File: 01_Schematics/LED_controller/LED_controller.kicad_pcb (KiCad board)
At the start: 2 copper layers, 122 x 87 mm, 221 parts, among them J1 Pin, J10 TB-02, J11 TB-02, J12 TB-03, J13 TB-02, J14 PLD-14, J15 PLD-14, J16 Pin, J17 Pin, J18 Pin, J19 Pin, J2 Pin, J20 TB-03, J21 TB-03, J22 Pin, J23 Pin, J24 Pin, J25 Pin, J26 Pin, J27 Pin, J28 PLD-14, J29 PLD-14, J3 TB-03, J30 Pin, J31 Pin, J32 Pin, J33 Pin, J34 TB-03, J35 TB-03, J36 Pin, J37 Pin, J38 Pin, J39 Pin, J4 Pin, J40 Pin, J41 Pin, J42 RJ45_LED_Shielded, J43 Pin, J44 Pin, J45 Pin, J46 Pin, J47 Pin, J48 PLS-4, J49 Pin, J5 Pin, J50 Pin, J51 Pin, J52 Pin, J53 Pin, J54 Pin, J55 Pin, J56 Pin, J57 Pin, J58 Pin, J59 Pin, J6 Pin, J60 Pin, J61 Pin, J62 Pin, J63 Pin, J64 Pin, J65 Pin, J66 Pin, J67 TB-02, J7 Pin, J7-2 Pin, J8 TB-02, J9 TB-03, K1 V23092-A1012-A301, Q1 MMBF170, U1 MC34063AD, U2 UA78L12ACPK, U3 MBI6651GSD, U4 MBI6651GSD, U5 MBI6651GSD, U6 MBI6651GSD, U7 DP83848C, U8 STM32F107RCTx, Y1 25 MHz

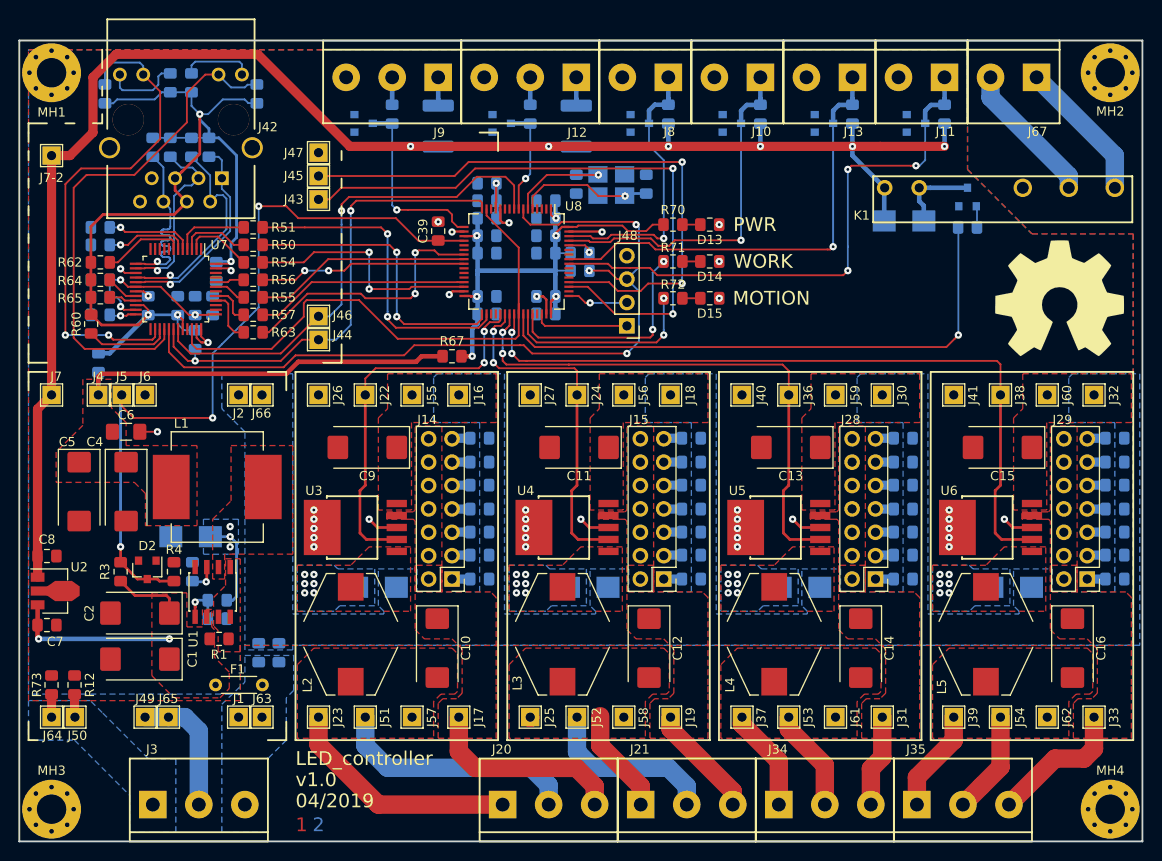
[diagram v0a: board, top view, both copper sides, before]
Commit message: - Исправлена ошибка с неправильным подключением цепи обратной связи микросхемы U1; - Плата переразведена с учетом изменений в схеме; - Добавлен файл BOM;
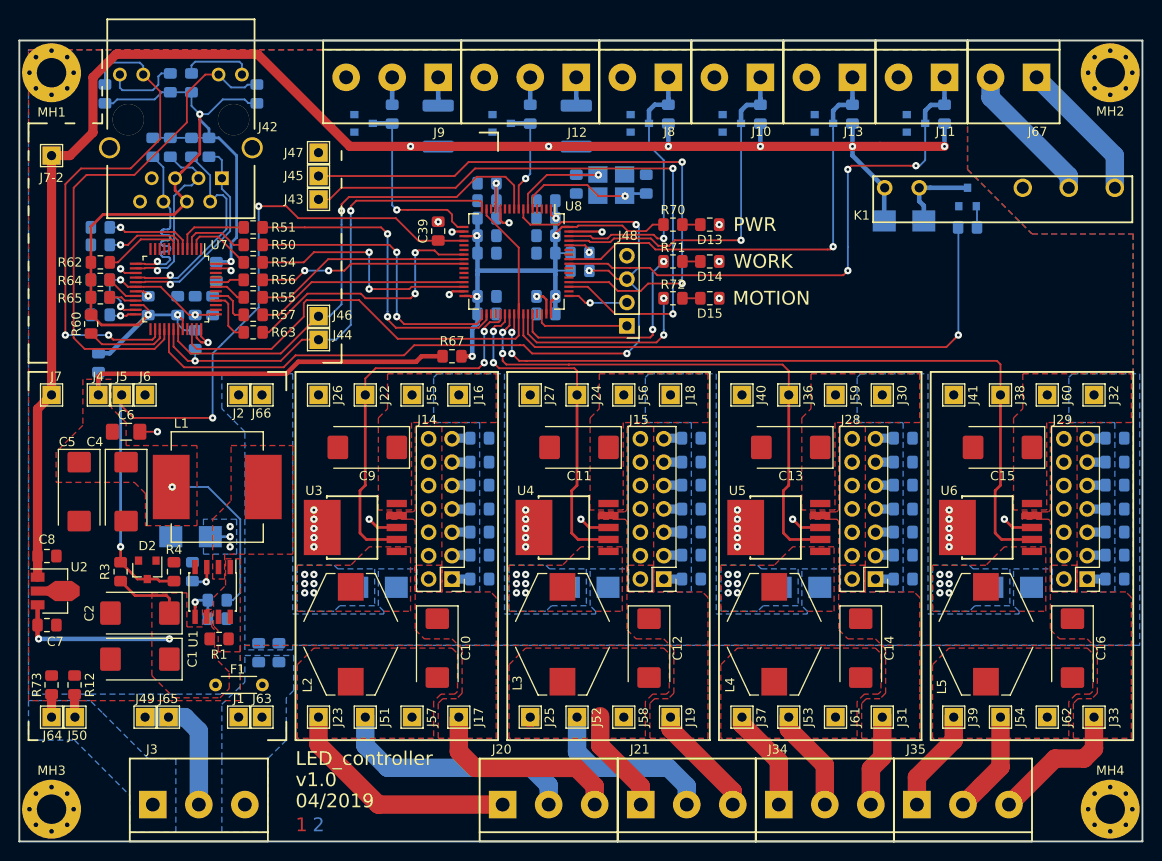
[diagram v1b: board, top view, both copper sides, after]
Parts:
- removed G***: OSHW_logo_14x14mm_silkscreen-front_14mm, extras:OSHW_logo_14x14mm_silkscreen-front_14mm
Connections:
- R5 pad 1: Net-(D1-Pad1) -> +3.3V
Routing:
- net +3.3V: track 42.8 -> 61.4 mm, vias 0 -> 1
- net Net-(D1-Pad1): track 10.2 -> 2.15 mm
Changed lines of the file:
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@@
     (thickness 1.6)
     (drawings 85)
-    (tracks 1098)
+    (tracks 1101)
     (zones 0)
-    (modules 221)
+    (modules 220)
     (nets 167)
   )
@@
       (net 91 "Net-(R5-Pad2)"))
     (pad 1 smd roundrect (at -1.025 0 180) (size 1.15 1.4) (layers B.Cu B.Paste B.Mask) (roundrect_rratio 0.217391)
-      (net 1 "Net-(D1-Pad1)"))
+      (net 2 +3.3V))
     (model ${KISYS3DMOD}/Resistor_SMD.3dshapes/R_0805_2012Metric.wrl
       (at (xyz 0 0 0))
@@
       (net 3 Vdrv))
   )
-  (module extras:OSHW_logo_14x14mm_silkscreen-front_14mm (layer F.Cu)
-    (at 163 78)
-    (fp_text reference G*** (at 0 7.42442) (layer F.SilkS) hide
-      (effects (font (size 0.63754 0.63754) (thickness 0.127)))
-    )
-    (fp_text value OSHW_logo_14x14mm_silkscreen-front_14mm (at 0 -7.42442) (layer F.SilkS) hide
-      (effects (font (size 0.63754 0.63754) (thickness 0.127)))
-    )
-    (fp_poly (pts (xy -4.24434 6.28904) (xy -4.17068 6.25094) (xy -4.00558 6.1468) (xy -3.7719 5.9944)
-      (xy -3.49758 5.80898) (xy -3.21818 5.62102) (xy -2.99212 5.46862) (xy -2.8321 5.36702)
-      (xy -2.76606 5.32892) (xy -2.72796 5.34162) (xy -2.59588 5.40512) (xy -2.40538 5.50418)
-      (xy -2.29616 5.5626) (xy -2.11836 5.6388) (xy -2.032 5.65404) (xy -2.01676 5.62864)
-      (xy -1.95326 5.49402) (xy -1.85166 5.26542) (xy -1.71958 4.96316) (xy -1.56972 4.60756)
-      (xy -1.40716 4.22402) (xy -1.2446 3.83286) (xy -1.08966 3.45948) (xy -0.9525 3.1242)
-      (xy -0.84328 2.85242) (xy -0.76962 2.66446) (xy -0.74422 2.58064) (xy -0.75184 2.5654)
-      (xy -0.84074 2.47904) (xy -0.99314 2.36474) (xy -1.32334 2.0955) (xy -1.651 1.68656)
-      (xy -1.85166 1.22428) (xy -1.9177 0.70866) (xy -1.85928 0.23114) (xy -1.67132 -0.2286)
-      (xy -1.35382 -0.64262) (xy -0.9652 -0.94742) (xy -0.51054 -1.143) (xy 0 -1.2065)
-      (xy 0.48768 -1.15062) (xy 0.95758 -0.9652) (xy 1.36906 -0.65024) (xy 1.54432 -0.44958)
-      (xy 1.78308 -0.03302) (xy 1.92024 0.41656) (xy 1.93548 0.53086) (xy 1.91516 1.02108)
-      (xy 1.77038 1.49352) (xy 1.5113 1.91516) (xy 1.15062 2.2606) (xy 1.1049 2.29362)
-      (xy 0.93726 2.41808) (xy 0.8255 2.50444) (xy 0.73914 2.57556) (xy 1.36398 4.08178)
-      (xy 1.46558 4.32308) (xy 1.63576 4.73456) (xy 1.78816 5.09016) (xy 1.90754 5.3721)
-      (xy 1.99136 5.56006) (xy 2.02946 5.63626) (xy 2.032 5.64134) (xy 2.08788 5.64896)
-      (xy 2.20218 5.60832) (xy 2.413 5.50672) (xy 2.5527 5.4356) (xy 2.71272 5.35686)
-      (xy 2.78384 5.32892) (xy 2.8448 5.36194) (xy 2.99974 5.461) (xy 3.22326 5.61086)
-      (xy 3.4925 5.79374) (xy 3.74904 5.969) (xy 3.98526 6.12394) (xy 4.15798 6.2357)
-      (xy 4.23926 6.27888) (xy 4.25196 6.27888) (xy 4.32816 6.23824) (xy 4.46278 6.12394)
-      (xy 4.66852 5.9309) (xy 4.95808 5.64388) (xy 5.0038 5.6007) (xy 5.24256 5.35686)
-      (xy 5.4356 5.15366) (xy 5.56514 5.00888) (xy 5.6134 4.94284) (xy 5.57022 4.86156)
-      (xy 5.461 4.68884) (xy 5.30352 4.45008) (xy 5.11302 4.17068) (xy 4.61518 3.44424)
-      (xy 4.8895 2.76098) (xy 4.97332 2.5527) (xy 5.08 2.29616) (xy 5.15874 2.11582)
-      (xy 5.19938 2.03708) (xy 5.27558 2.00914) (xy 5.461 1.96596) (xy 5.73278 1.91008)
-      (xy 6.0579 1.84912) (xy 6.36524 1.7907) (xy 6.64464 1.7399) (xy 6.8453 1.69926)
-      (xy 6.93674 1.68148) (xy 6.95706 1.66878) (xy 6.97484 1.6256) (xy 6.98754 1.53162)
-      (xy 6.99516 1.36144) (xy 6.9977 1.09474) (xy 6.9977 0.70866) (xy 6.9977 0.66802)
-      (xy 6.99516 0.29718) (xy 6.98754 0.00508) (xy 6.97738 -0.18796) (xy 6.96468 -0.26416)
-      (xy 6.87832 -0.28448) (xy 6.6802 -0.32766) (xy 6.40334 -0.381) (xy 6.0706 -0.4445)
-      (xy 6.05028 -0.44958) (xy 5.71754 -0.51308) (xy 5.44068 -0.56896) (xy 5.24764 -0.61468)
-      (xy 5.16382 -0.64008) (xy 5.14858 -0.66294) (xy 5.08 -0.79248) (xy 4.98602 -0.99822)
-      (xy 4.8768 -1.24968) (xy 4.76758 -1.50876) (xy 4.6736 -1.74244) (xy 4.61264 -1.9177)
-      (xy 4.59232 -1.99644) (xy 4.59232 -1.99898) (xy 4.64312 -2.07772) (xy 4.75742 -2.2479)
-      (xy 4.91744 -2.48666) (xy 5.11048 -2.7686) (xy 5.12572 -2.79146) (xy 5.31622 -3.07086)
-      (xy 5.47116 -3.30708) (xy 5.57276 -3.47726) (xy 5.6134 -3.55092) (xy 5.61086 -3.556)
-      (xy 5.54736 -3.63982) (xy 5.40512 -3.79984) (xy 5.20192 -4.0132) (xy 4.95554 -4.25958)
-      (xy 4.87934 -4.33578) (xy 4.60756 -4.60248) (xy 4.41706 -4.7752) (xy 4.30022 -4.86918)
-      (xy 4.24434 -4.8895) (xy 4.2418 -4.88696) (xy 4.15798 -4.83616) (xy 3.98018 -4.72186)
-      (xy 3.74142 -4.5593) (xy 3.45694 -4.36626) (xy 3.43662 -4.35356) (xy 3.15722 -4.16306)
-      (xy 2.92354 -4.00558) (xy 2.75844 -3.89382) (xy 2.68732 -3.85064) (xy 2.67462 -3.85064)
-      (xy 2.56032 -3.88366) (xy 2.3622 -3.95478) (xy 2.11582 -4.04876) (xy 1.85674 -4.1529)
-      (xy 1.62306 -4.25196) (xy 1.44526 -4.33324) (xy 1.36144 -4.37896) (xy 1.3589 -4.38404)
-      (xy 1.33096 -4.48564) (xy 1.2827 -4.69392) (xy 1.22174 -4.98348) (xy 1.15824 -5.32384)
-      (xy 1.14808 -5.37972) (xy 1.08458 -5.71246) (xy 1.03124 -5.98932) (xy 0.9906 -6.17982)
-      (xy 0.97282 -6.25856) (xy 0.92456 -6.26872) (xy 0.762 -6.28142) (xy 0.51308 -6.2865)
-      (xy 0.21082 -6.29158) (xy -0.10668 -6.28904) (xy -0.41656 -6.28142) (xy -0.68072 -6.27126)
-      (xy -0.86868 -6.25856) (xy -0.94742 -6.24332) (xy -0.94996 -6.23824) (xy -0.98044 -6.13664)
-      (xy -1.02616 -5.92582) (xy -1.08458 -5.63626) (xy -1.15062 -5.29336) (xy -1.16078 -5.2324)
-      (xy -1.22428 -4.89966) (xy -1.28016 -4.62534) (xy -1.3208 -4.43992) (xy -1.34112 -4.36626)
-      (xy -1.3716 -4.34848) (xy -1.50876 -4.29006) (xy -1.73228 -4.19608) (xy -2.00914 -4.08432)
-      (xy -2.64922 -3.82524) (xy -3.43408 -4.36372) (xy -3.50774 -4.41198) (xy -3.78968 -4.60502)
-      (xy -4.02082 -4.75996) (xy -4.18338 -4.8641) (xy -4.24942 -4.9022) (xy -4.2545 -4.89966)
-      (xy -4.33324 -4.83108) (xy -4.49072 -4.68376) (xy -4.70154 -4.47802) (xy -4.95046 -4.23164)
-      (xy -5.13334 -4.04876) (xy -5.34924 -3.82778) (xy -5.4864 -3.68046) (xy -5.56006 -3.58394)
-      (xy -5.588 -3.52806) (xy -5.58038 -3.48996) (xy -5.52958 -3.40868) (xy -5.41528 -3.23596)
-      (xy -5.25272 -2.9972) (xy -5.06222 -2.72034) (xy -4.90474 -2.48666) (xy -4.73456 -2.2225)
-      (xy -4.6228 -2.03454) (xy -4.5847 -1.9431) (xy -4.59486 -1.905) (xy -4.6482 -1.75006)
-      (xy -4.74218 -1.51892) (xy -4.86156 -1.24206) (xy -5.13334 -0.61976) (xy -5.54228 -0.54102)
-      (xy -5.78866 -0.4953) (xy -6.1341 -0.42926) (xy -6.4643 -0.36322) (xy -6.97992 -0.26416)
-      (xy -7.00024 1.63322) (xy -6.91896 1.66878) (xy -6.84276 1.6891) (xy -6.65226 1.72974)
-      (xy -6.37794 1.78562) (xy -6.0579 1.84658) (xy -5.78104 1.89738) (xy -5.50672 1.95072)
-      (xy -5.3086 1.98882) (xy -5.2197 2.0066) (xy -5.19684 2.03708) (xy -5.12826 2.1717)
-      (xy -5.0292 2.38252) (xy -4.91998 2.63906) (xy -4.80822 2.90576) (xy -4.7117 3.1496)
-      (xy -4.64312 3.33756) (xy -4.61772 3.43408) (xy -4.65582 3.5052) (xy -4.75996 3.66776)
-      (xy -4.91236 3.90144) (xy -5.10032 4.17576) (xy -5.28828 4.45008) (xy -5.4483 4.68376)
-      (xy -5.55752 4.85394) (xy -5.60324 4.93014) (xy -5.58038 4.98348) (xy -5.47116 5.11556)
-      (xy -5.26288 5.33146) (xy -4.95554 5.63626) (xy -4.90474 5.68706) (xy -4.65836 5.92074)
-      (xy -4.45262 6.11124) (xy -4.30784 6.24078) (xy -4.24434 6.28904)) (layer F.SilkS) (width 0.00254))
-  )
   (dimension 87 (width 0.3) (layer Dwgs.User)
     (gr_text "87,000 mm" (at 178.1 93.5 270) (layer Dwgs.User)
@@
   (gr_line (start 50 50) (end 172 50) (layer Edge.Cuts) (width 0.2))
   (segment (start 72.9 103.9) (end 72.9 103.9) (width 0.3) (layer B.Cu) (net 1))
-  (segment (start 73.6 104.6) (end 72.9 103.9) (width 0.3) (layer B.Cu) (net 1))
-  (segment (start 73.6 110.4) (end 73.6 104.6) (width 0.3) (layer B.Cu) (net 1))
-  (segment (start 72.525 110.8) (end 73.2 110.8) (width 0.3) (layer B.Cu) (net 1))
-  (segment (start 73.2 110.8) (end 73.6 110.4) (width 0.3) (layer B.Cu) (net 1))
   (segment (start 72.9 103.9) (end 70.75 103.9) (width 0.3) (layer B.Cu) (net 1))
   (via (at 72.9 103.9) (size 0.8) (drill 0.3) (layers F.Cu B.Cu) (net 1))
@@
   (segment (start 79 86.2) (end 80.3 84.9) (width 0.5) (layer F.Cu) (net 2))
   (segment (start 80.3 84.9) (end 93.1 84.9) (width 0.5) (layer F.Cu) (net 2))
+  (segment (start 66.6 98.5) (end 66.6 98.5) (width 0.2) (layer B.Cu) (net 2))
+  (via (at 66.6 98.5) (size 0.8) (drill 0.3) (layers F.Cu B.Cu) (net 2))
+  (segment (start 70.5 98.5) (end 66.6 98.5) (width 0.2) (layer B.Cu) (net 2))
+  (segment (start 74 102) (end 70.5 98.5) (width 0.2) (layer B.Cu) (net 2))
+  (segment (start 72.525 110.8) (end 73.2 110.8) (width 0.2) (layer B.Cu) (net 2))
+  (segment (start 74 110) (end 74 102) (width 0.2) (layer B.Cu) (net 2))
+  (segment (start 73.2 110.8) (end 74 110) (width 0.2) (layer B.Cu) (net 2))
   (segment (start 66.8 108.725) (end 65.225 108.725) (width 0.3) (layer F.Cu) (net 5))
   (segment (start 65 108.5) (end 63.9 108.5) (width 0.3) (layer F.Cu) (net 5))
@@
     (polygon
       (pts
-        (xy 70 102) (xy 70 105.8) (xy 73.8 105.8) (xy 73.8 102)
+        (xy 70 102) (xy 70 105.8) (xy 73.6 105.8) (xy 73.6 102)
       )
     )
